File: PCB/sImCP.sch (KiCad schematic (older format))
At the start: 79 parts, among them J1 AVR-ISP-6, SW1 RESET, SW2 BOOT, U1 ATmega328P-AU, Y1 16MHz

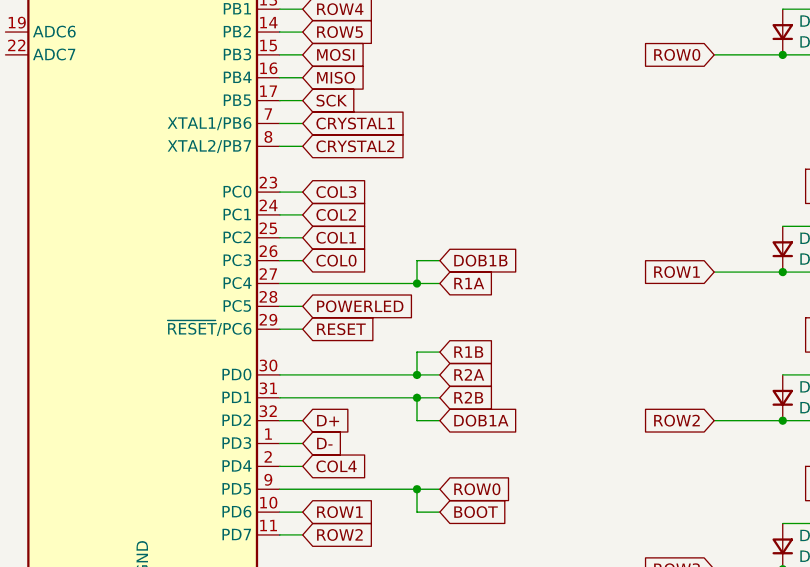
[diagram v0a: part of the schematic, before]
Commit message: rerouted with new encoder wiring
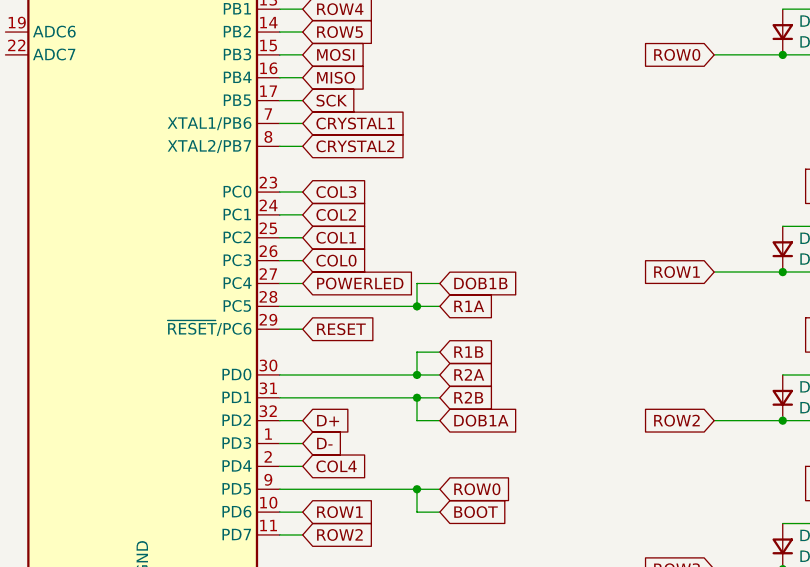
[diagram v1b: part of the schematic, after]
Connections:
- net DOB1B: now also U1.28 (PC5); no longer U1.27 (PC4)
- net POWERLED: now also U1.27 (PC4); no longer U1.28 (PC5)
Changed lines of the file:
@@
 Wire Wire Line
 	2450 2400 2550 2400
-Text GLabel 3150 2500 2    50   Input ~ 0
+Text GLabel 3150 2600 2    50   Input ~ 0
 R1A
 Text GLabel 3150 2800 2    50   Input ~ 0
@@
 R2B
 Wire Wire Line
-	2550 2600 2450 2600
+	2550 2500 2450 2500
 Text GLabel 3150 3100 2    50   Input ~ 0
 DOB1A
-Text GLabel 3150 2400 2    50   Input ~ 0
+Text GLabel 3150 2500 2    50   Input ~ 0
 DOB1B
 $Comp
@@
 	3050 2800 3150 2800
 Wire Wire Line
-	3050 2500 3050 2400
-Wire Wire Line
-	3050 2400 3150 2400
+	3050 2600 3050 2500
 Wire Wire Line
 	3050 2500 3150 2500
 Wire Wire Line
-	2450 2500 3050 2500
-Connection ~ 3050 2500
+	3050 2600 3150 2600
+Wire Wire Line
+	2450 2600 3050 2600
+Connection ~ 3050 2600
 Wire Wire Line
 	2450 2900 3050 2900
@@
 Wire Wire Line
 	10350 6000 10250 6000
-Text GLabel 2550 2600 2    50   Input ~ 0
+Text GLabel 2550 2500 2    50   Input ~ 0
 POWERLED
 Wire Wire Line

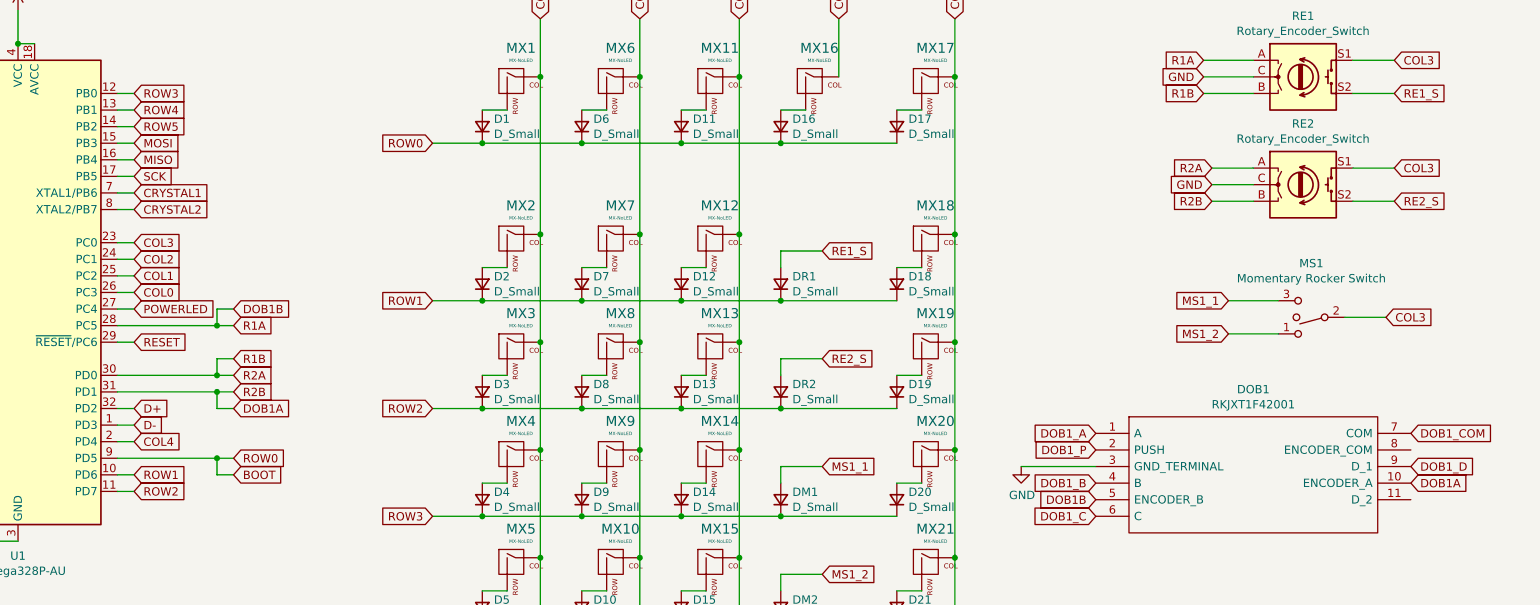
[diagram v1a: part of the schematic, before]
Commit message: fixed encoders mess, wiring missing
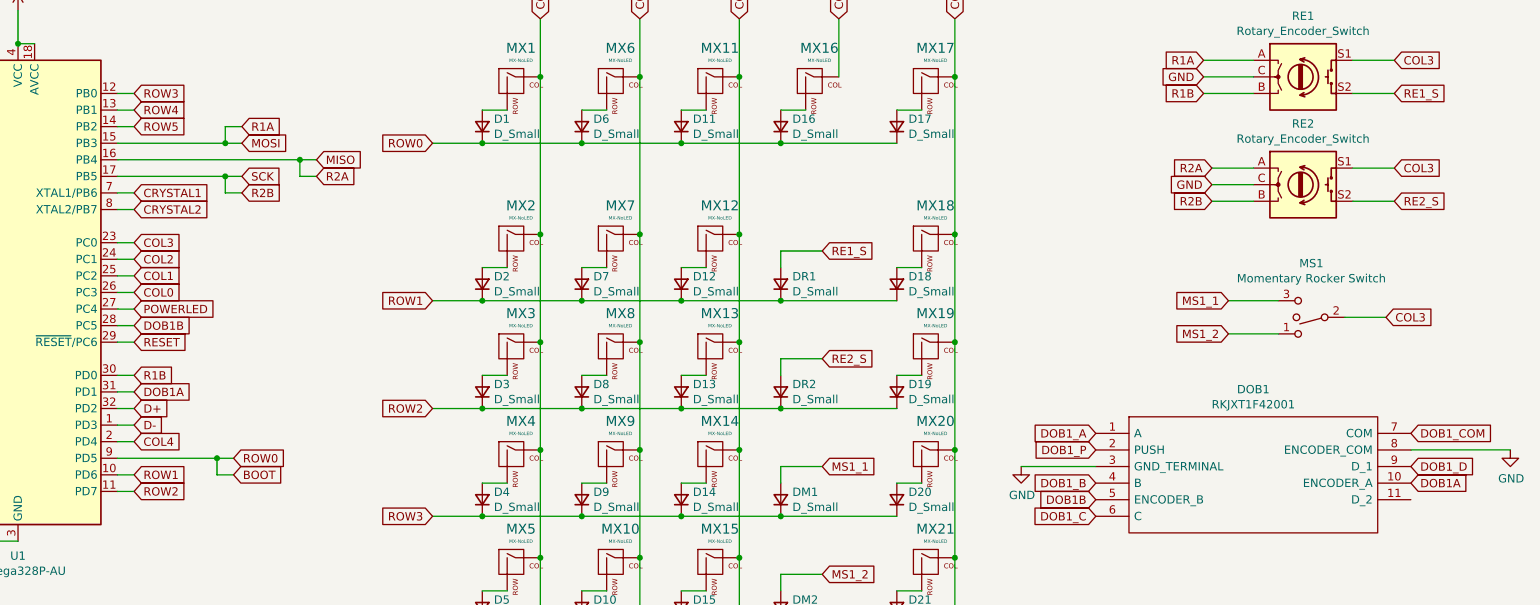
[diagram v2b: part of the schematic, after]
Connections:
- net DOB1A: no longer RE2.B
- net DOB1B: no longer RE1.A
- net GND: now also DOB1.8 (ENCODER_COM)
- net MISO: now also RE2.A
- net MOSI: now also RE1.A
- net R1B: no longer RE2.A
- net SCK renamed R2B
- net R2B: now also RE2.B
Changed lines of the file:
@@
 Wire Wire Line
 	2550 2700 2450 2700
-Text GLabel 2550 1500 2    50   Input ~ 0
+Text GLabel 3200 1500 2    50   Input ~ 0
 MOSI
-Text GLabel 2550 1600 2    50   Input ~ 0
+Text GLabel 3650 1600 2    50   Input ~ 0
 MISO
-Wire Wire Line
-	2550 1700 2450 1700
 $Comp
 L power:GND #PWR0115
@@
 Wire Wire Line
 	2450 2400 2550 2400
-Text GLabel 3150 2600 2    50   Input ~ 0
+Text GLabel 3200 1400 2    50   Input ~ 0
 R1A
-Text GLabel 3150 2800 2    50   Input ~ 0
+Text GLabel 2550 2900 2    50   Input ~ 0
 R1B
-Text GLabel 3150 2900 2    50   Input ~ 0
+Text GLabel 3650 1700 2    50   Input ~ 0
 R2A
-Text GLabel 3150 3000 2    50   Input ~ 0
+Text GLabel 3200 1800 2    50   Input ~ 0
 R2B
 Wire Wire Line
 	2550 2500 2450 2500
-Text GLabel 3150 3100 2    50   Input ~ 0
+Text GLabel 2550 3000 2    50   Input ~ 0
 DOB1A
-Text GLabel 3150 2500 2    50   Input ~ 0
+Text GLabel 2550 2600 2    50   Input ~ 0
 DOB1B
 $Comp
@@
 	1    0    0    -1
 $EndComp
-Wire Wire Line
-	2450 1600 2550 1600
-Text GLabel 2550 1700 2    50   Input ~ 0
+Text GLabel 3200 1700 2    50   Input ~ 0
 SCK
-Wire Wire Line
-	2550 1500 2450 1500
-Wire Wire Line
-	3150 3100 3050 3100
-Wire Wire Line
-	3050 3100 3050 3000
-Wire Wire Line
-	3050 3000 3150 3000
-Wire Wire Line
-	3150 2900 3050 2900
-Wire Wire Line
-	3050 2900 3050 2800
-Wire Wire Line
-	3050 2800 3150 2800
-Wire Wire Line
-	3050 2600 3050 2500
-Wire Wire Line
-	3050 2500 3150 2500
-Wire Wire Line
-	3050 2600 3150 2600
-Wire Wire Line
-	2450 2600 3050 2600
-Connection ~ 3050 2600
-Wire Wire Line
-	2450 2900 3050 2900
-Connection ~ 3050 2900
-Wire Wire Line
-	2450 3000 3050 3000
-Connection ~ 3050 3000
 Text GLabel 10350 6000 2    50   Input ~ 0
 POWERLED
 Wire Wire Line
 	10350 6000 10250 6000
+Wire Wire Line
+	3150 3400 3050 3400
+Wire Wire Line
+	3050 3400 3050 3500
+Wire Wire Line
+	3050 3500 3150 3500
+Wire Wire Line
+	3050 3400 2450 3400
+Connection ~ 3050 3400
+$Comp
+L power:GND #PWR0119
+U 1 1 60B8A9AB
+P 10850 3350
+F 0 "#PWR0119" H 10850 3100 50  0001 C CNN
+F 1 "GND" H 10855 3177 50  0000 C CNN
+F 2 "" H 10850 3350 50  0001 C CNN
+F 3 "" H 10850 3350 50  0001 C CNN
+	1    10850 3350
+	1    0    0    -1
+$EndComp
+Wire Wire Line
+	10850 3350 10250 3350
+Wire Wire Line
+	2550 2900 2450 2900
+Wire Wire Line
+	2550 3000 2450 3000
+Wire Wire Line
+	2450 1500 3100 1500
+Wire Wire Line
+	2450 1600 3550 1600
+Wire Wire Line
+	3650 1700 3550 1700
+Wire Wire Line
+	3550 1700 3550 1600
+Connection ~ 3550 1600
+Wire Wire Line
+	3550 1600 3650 1600
+Wire Wire Line
+	3200 1400 3100 1400
+Wire Wire Line
+	3100 1400 3100 1500
+Connection ~ 3100 1500
+Wire Wire Line
+	3100 1500 3200 1500
+Wire Wire Line
+	2450 1700 3100 1700
+Wire Wire Line
+	3200 1800 3100 1800
+Wire Wire Line
+	3100 1800 3100 1700
+Connection ~ 3100 1700
+Wire Wire Line
+	3100 1700 3200 1700
 Text GLabel 2550 2500 2    50   Input ~ 0
 POWERLED
 Wire Wire Line
-	3150 3400 3050 3400
-Wire Wire Line
-	3050 3400 3050 3500
-Wire Wire Line
-	3050 3500 3150 3500
-Wire Wire Line
-	3050 3400 2450 3400
-Connection ~ 3050 3400
+	2550 2600 2450 2600
 $EndSCHEMATC

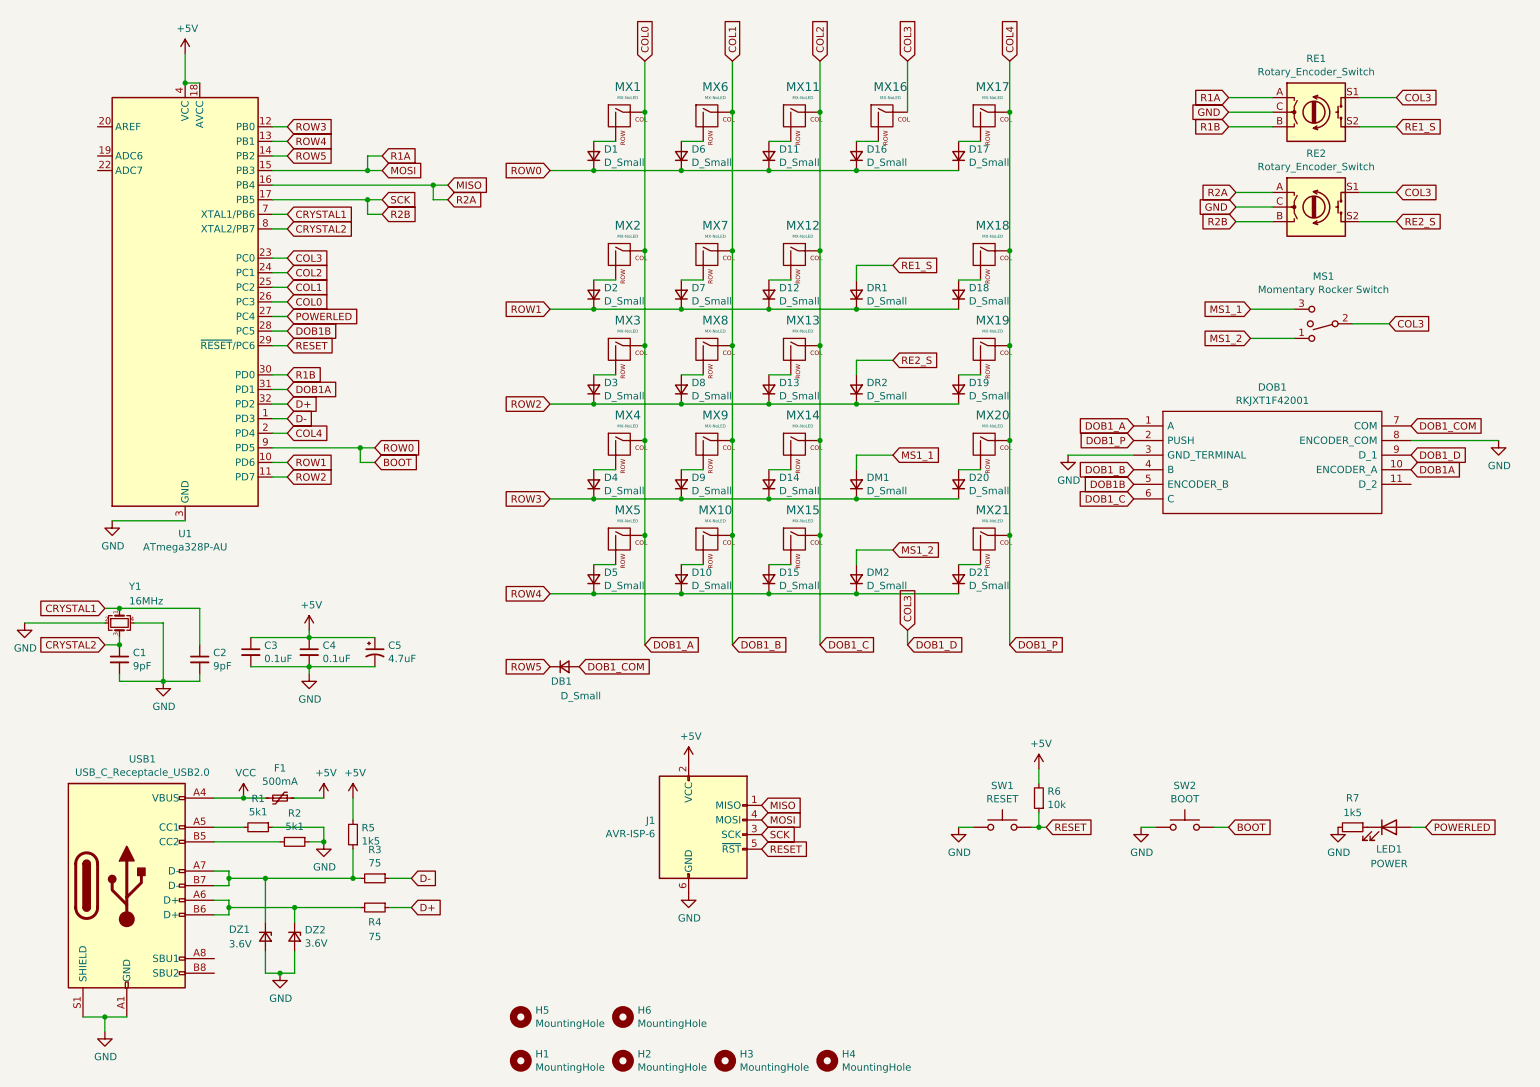
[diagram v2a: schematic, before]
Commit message: added backlight leds and control mosfet
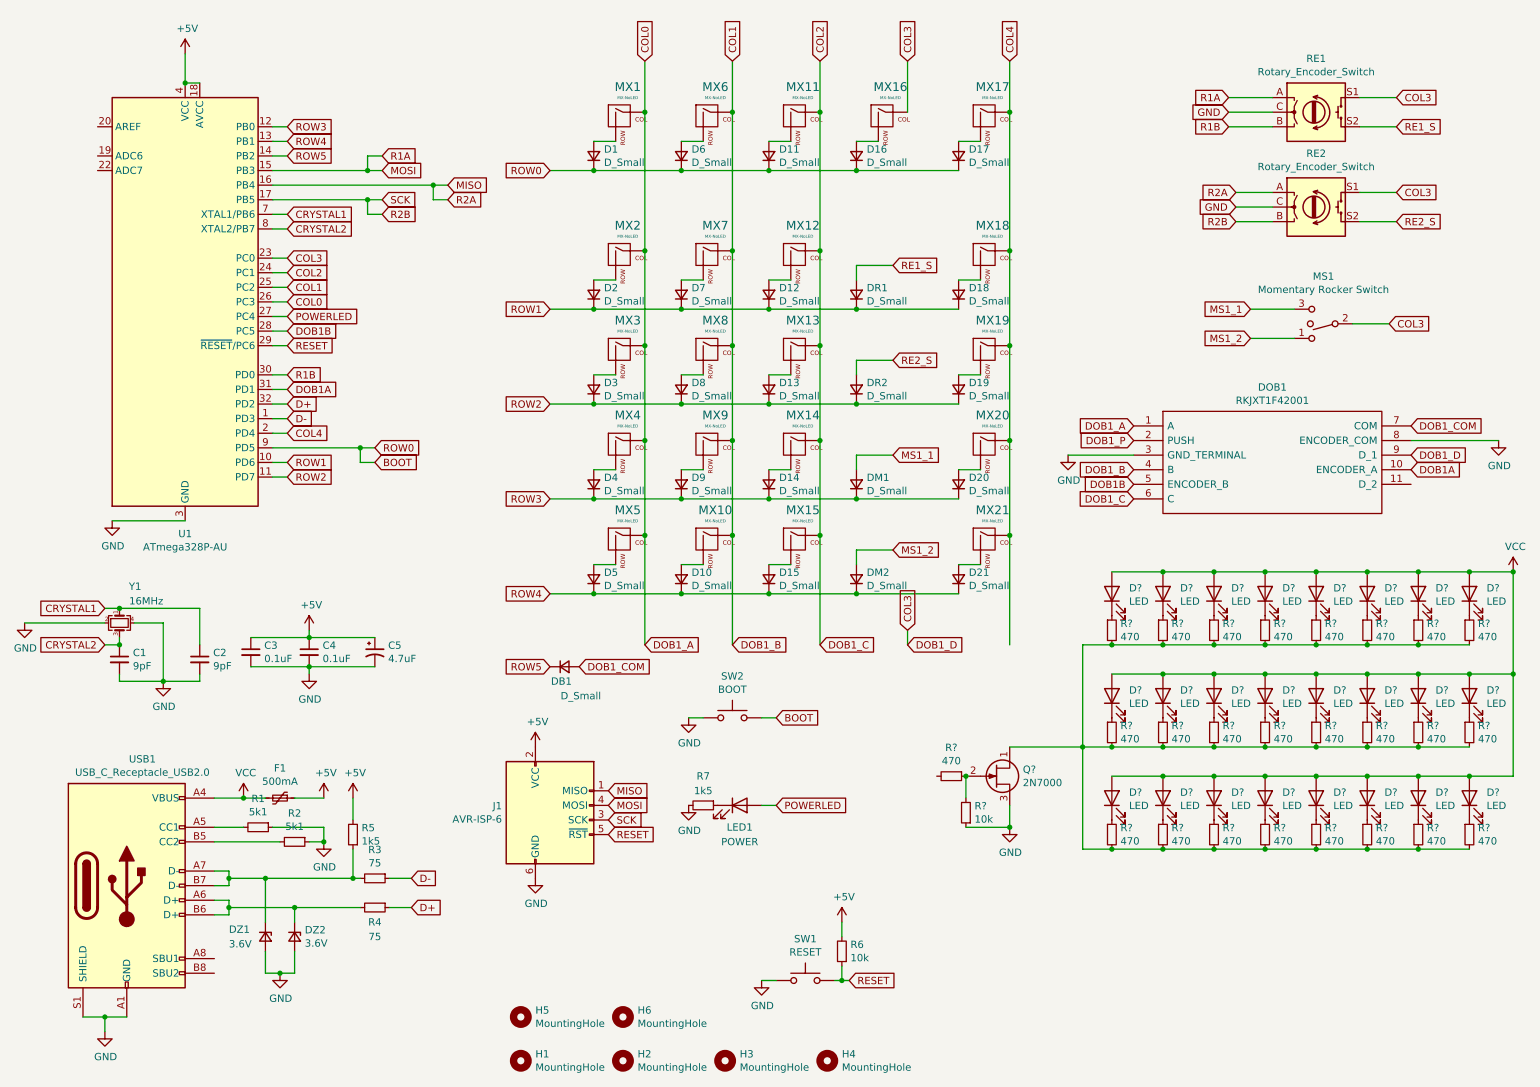
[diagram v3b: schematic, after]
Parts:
- added D? (x24): LED, symbol Device:LED
- added Q?: 2N7000, Package_TO_SOT_THT:TO-92_Inline, symbol Transistor_FET:BF244B
- added R? (x25): 470, symbol Device:R_Small
- added R?: 10k, symbol Device:R_Small
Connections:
- net COL4: no longer DOB1.2 (PUSH)
- net GND: now also Q?.3 (S), R?.1
- net VCC: now also D?.2 (A), D?.2 (A), D?.2 (A), D?.2 (A), D?.2 (A), D?.2 (A), D?.2 (A), D?.2 (A), D?.2 (A), D?.2 (A), D?.2 (A), D?.2 (A), D?.2 (A), D?.2 (A), D?.2 (A), D?.2 (A), D?.2 (A), D?.2 (A), D?.2 (A), D?.2 (A), D?.2 (A), D?.2 (A), D?.2 (A), D?.2 (A)
- new net: D?.1 (K), R?.1 (x24)
- new net: Q?.1 (D), R?.2, R?.2, R?.2, R?.2, R?.2, R?.2, R?.2, R?.2, R?.2, R?.2, R?.2, R?.2, R?.2, R?.2, R?.2, R?.2, R?.2, R?.2, R?.2, R?.2, R?.2, R?.2, R?.2, R?.2
- new net: Q?.2 (G), R?.1, R?.2
- new net DOB1_P: DOB1.2 (PUSH)
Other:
- moved on the sheet: J1, LED1, R6, R7, SW1, SW2
